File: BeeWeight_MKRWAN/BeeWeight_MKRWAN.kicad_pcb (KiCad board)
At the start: 2 copper layers, 38.6 x 67.9 mm, 34 parts, among them J2 691412120004B, J3 691412120004B, J4 691412120004B, J5 691412120004B, J6 Conn_01x02_Male, J7 Conn_01x14_Female, J8 Conn_01x14_Female, J9 694108301002, Q1 IRLML2244, U1 ADS1241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

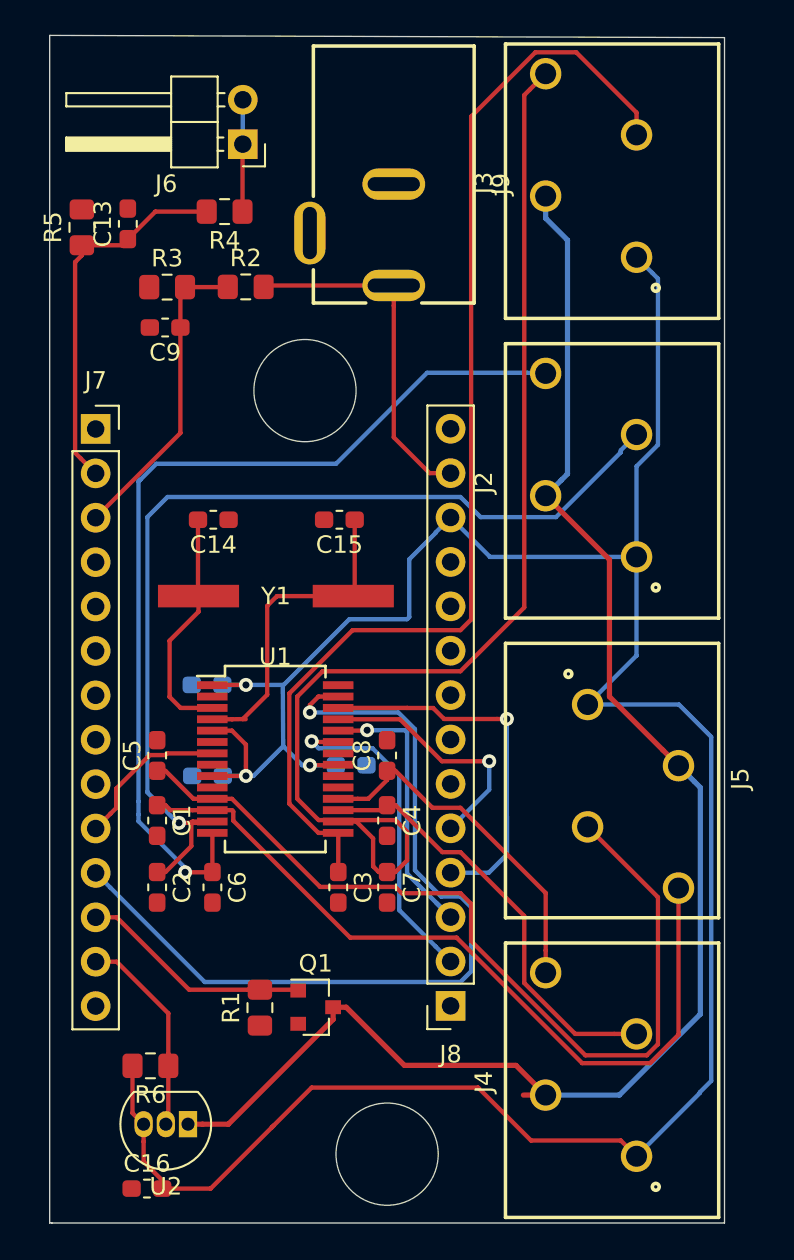
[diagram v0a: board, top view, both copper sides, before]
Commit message: Update Crystal Footprint
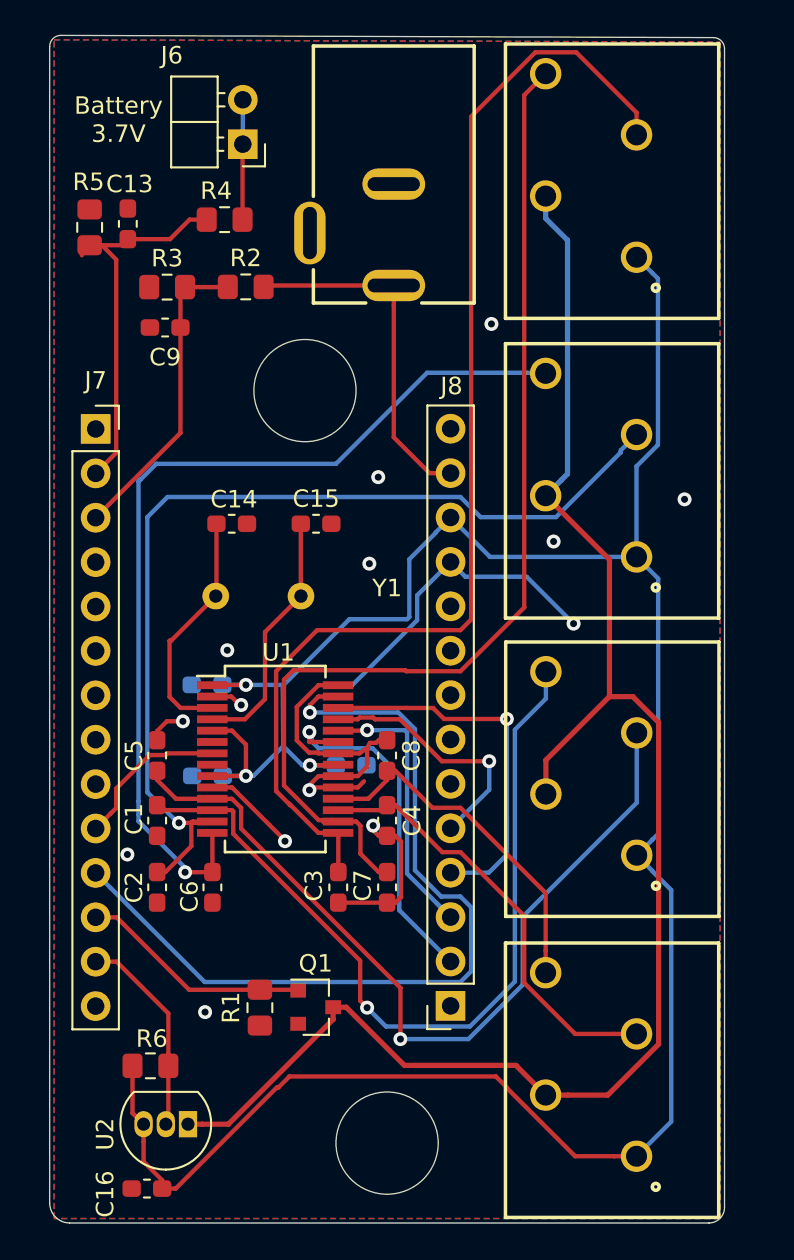
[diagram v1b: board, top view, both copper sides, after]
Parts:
- Y1: footprint USMB_Syl_Mont:Crystal_4Mhz_MCRSD04000F183000RR -> USMB_Syl_Mont:Crystal-4Mhz-TH-Wurth-830027298B
- moved J5 3.04 mm to (182.0, 91.3), turned to 90 degrees
- moved C15 1.35 mm to (166.2, 77.6), turned to 0 degrees
- moved C14 1.08 mm to (161.4, 77.6)
- moved Y1 1.00 mm to (162.9, 81.7)
- moved R4 0.46 mm to (161.0, 60.2)
- moved R5 0.44 mm to (153.3, 60.6)
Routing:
- net GND: track 0.21 -> 56.8 mm, vias 0 -> 14
- net /3V3: track 151.7 -> 145.8 mm
- net /AIN7: track 67.0 -> 61.5 mm
- net /GND_LowPower: track 89.3 -> 93.5 mm
- net Net-(C15-Pad1): track 18.5 -> 14.4 mm
- net /AIN0: track 51.0 -> 48.4 mm, vias 0 -> 1
- net /AIN6: track 66.7 -> 68.7 mm
- net /AIN1: track 45.3 -> 47.3 mm, vias 0 -> 1
- net /D7_CS: track 19.2 -> 20.6 mm
- net /A0_D15_3V7_BAT: track 21.6 -> 22.9 mm
- added copper zone on B.Cu, net GND
- added copper zone on F.Cu, net GND
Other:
- outline, holes or cut-outs redrawn
- board text added: "AIN0"
- board text added: "AIN1"
- board text added: "AIN2"
- board text added: "AIN3"
- board text added: "AIN4"
- board text added: "AIN5"
- board text added: "AIN6"
- board text added: "AIN7"
- board text added: "Alim+"
- board text added: "Alim-"
- board text added: "Battery 3.7V"
- board text added: "Bee Weight MKRWAN Univ Savoie Mont Blanc Version 1"
- board text added: "Diff+"
- board text added: "Diff-"
- board text added: "Solar Panel"

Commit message: Minor changes in schematic and PCB
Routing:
- net /D2_DRDY: track 48.8 -> 46.3 mm
- net /3V3: track 145.8 -> 143.9 mm
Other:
- board text added: "Solar Panel or 4V-17V DC"
- board text removed: "Solar Panel"
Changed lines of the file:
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@@
     (thickness 1.6)
     (drawings 44)
-    (tracks 385)
+    (tracks 384)
     (zones 0)
     (modules 34)
@@
   (layers
     (0 F.Cu signal)
-    (31 B.Cu signal)
+    (31 B.Cu signal hide)
     (32 B.Adhes user)
     (33 F.Adhes user)
@@
     (effects (font (size 1 1) (thickness 0.15)))
   )
-  (gr_text "Solar Panel" (at 170.307 51.943) (layer B.SilkS)
+  (gr_text "Solar Panel\nor\n4V-17V DC" (at 170.688 53.721) (layer B.SilkS)
     (effects (font (size 1 1) (thickness 0.15)) (justify mirror))
   )
@@
   (segment (start 160.3062 92.684) (end 161.4312 92.684) (width 0.25) (layer F.Cu) (net 1))
   (segment (start 161.4312 92.684) (end 164.465 95.7178) (width 0.25) (layer F.Cu) (net 1))
-  (segment (start 172.027009 83.117401) (end 168.27641 86.868) (width 0.25) (layer B.Cu) (net 1))
   (segment (start 173.9392 79.7814) (end 172.02701 81.69359) (width 0.25) (layer B.Cu) (net 1))
-  (segment (start 172.02701 81.69359) (end 172.027009 83.117401) (width 0.25) (layer B.Cu) (net 1))
   (segment (start 168.27641 86.868) (end 167.64 86.868) (width 0.25) (layer B.Cu) (net 1))
   (segment (start 170.307 90.3582) (end 170.307 89.9808) (width 0.25) (layer F.Cu) (net 1))
@@
   (segment (start 168.6312 92.684) (end 168.9862 92.329) (width 0.25) (layer F.Cu) (net 1))
   (segment (start 167.5062 92.684) (end 168.6312 92.684) (width 0.25) (layer F.Cu) (net 1))
+  (segment (start 172.02701 81.69359) (end 172.02701 81.71899) (width 0.25) (layer B.Cu) (net 1))
+  (segment (start 172.02701 81.71899) (end 168.91 84.836) (width 0.25) (layer B.Cu) (net 1))
+  (segment (start 168.91 84.836) (end 168.91 86.36) (width 0.25) (layer B.Cu) (net 1))
+  (segment (start 168.91 86.36) (end 168.27641 86.868) (width 0.25) (layer B.Cu) (net 1))
   (segment (start 175.049201 106.356401) (end 170.237401 106.356401) (width 0.25) (layer B.Cu) (net 2))
   (segment (start 177.61501 103.790592) (end 175.049201 106.356401) (width 0.25) (layer B.Cu) (net 2))
@@
   (segment (start 162.2298 90.2326) (end 162.2298 91.458515) (width 0.25) (layer F.Cu) (net 11))
   (segment (start 160.3062 89.434) (end 161.4312 89.434) (width 0.25) (layer F.Cu) (net 11))
-  (segment (start 173.089201 78.091399) (end 173.089201 78.116799) (width 0.25) (layer B.Cu) (net 11))
-  (segment (start 173.9392 77.2414) (end 173.089201 78.091399) (width 0.25) (layer B.Cu) (net 11))
-  (segment (start 173.089201 78.116799) (end 171.577 79.629) (width 0.25) (layer B.Cu) (net 11))
-  (segment (start 171.577 79.629) (end 171.577 82.931) (width 0.25) (layer B.Cu) (net 11))
-  (segment (start 171.577 82.931) (end 171.45 83.058) (width 0.25) (layer B.Cu) (net 11))
-  (segment (start 171.45 83.058) (end 168.148 83.058) (width 0.25) (layer B.Cu) (net 11))
-  (segment (start 168.148 83.058) (end 164.338 86.868) (width 0.25) (layer B.Cu) (net 11))
   (segment (start 164.3634 86.8172) (end 164.338 86.868) (width 0.25) (layer B.Cu) (net 11))
   (segment (start 164.338 86.868) (end 164.3634 90.3224) (width 0.25) (layer B.Cu) (net 11))
@@
   (segment (start 164.719 109.22) (end 176.53 109.22) (width 0.25) (layer F.Cu) (net 11))
   (segment (start 177.165 109.855) (end 177.136098 109.855) (width 0.25) (layer F.Cu) (net 11))
+  (segment (start 173.089201 78.116799) (end 168.148 83.058) (width 0.25) (layer B.Cu) (net 11))
+  (segment (start 173.9392 77.2414) (end 173.089201 78.091399) (width 0.25) (layer B.Cu) (net 11))
+  (segment (start 168.148 83.058) (end 164.338 86.868) (width 0.25) (layer B.Cu) (net 11))
+  (segment (start 173.089201 78.091399) (end 173.089201 78.116799) (width 0.25) (layer B.Cu) (net 11))
   (segment (start 155.1234 61.6643) (end 155.4734 61.3143) (width 0.25) (layer F.Cu) (net 12))
   (segment (start 152.8445 61.6643) (end 155.1234 61.6643) (width 0.25) (layer F.Cu) (net 12))
@@
   (segment (start 154.806901 92.753189) (end 154.806901 93.859099) (width 0.25) (layer F.Cu) (net 24))
   (segment (start 160.3062 90.734) (end 157.71711 90.734) (width 0.25) (layer F.Cu) (net 24))
-  (segment (start 166.3812 87.484) (end 166.3622 87.503) (width 0.25) (layer F.Cu) (net 25))
-  (segment (start 167.5062 87.484) (end 166.3812 87.484) (width 0.25) (layer F.Cu) (net 25))
-  (via (at 165.887399 88.392) (size 0.8) (drill 0.4) (layers F.Cu B.Cu) (net 25))
-  (segment (start 166.3622 87.503) (end 165.887399 87.977801) (width 0.25) (layer F.Cu) (net 25))
-  (segment (start 165.887399 87.977801) (end 165.887399 88.392) (width 0.25) (layer F.Cu) (net 25))
   (segment (start 175.114201 103.205401) (end 174.503201 103.816401) (width 0.25) (layer B.Cu) (net 25))
   (segment (start 159.874201 103.816401) (end 154.481899 98.424099) (width 0.25) (layer B.Cu) (net 25))
@@
   (segment (start 174.503201 103.816401) (end 159.874201 103.816401) (width 0.25) (layer B.Cu) (net 25))
   (segment (start 171.90001 89.3486) (end 171.90001 97.4258) (width 0.25) (layer B.Cu) (net 25))
-  (segment (start 170.94341 88.392) (end 171.90001 89.3486) (width 0.25) (layer B.Cu) (net 25))
   (segment (start 154.481899 98.424099) (end 153.6319 97.5741) (width 0.25) (layer B.Cu) (net 25))
-  (segment (start 165.887399 88.392) (end 170.94341 88.392) (width 0.25) (layer B.Cu) (net 25))
+  (segment (start 167.5062 87.484) (end 171.431 87.484) (width 0.25) (layer F.Cu) (net 25))
+  (via (at 171.47844 87.409726) (size 0.8) (drill 0.4) (layers F.Cu B.Cu) (net 25))
+  (segment (start 171.431 87.484) (end 171.431 87.457166) (width 0.25) (layer F.Cu) (net 25))
+  (segment (start 171.431 87.457166) (end 171.47844 87.409726) (width 0.25) (layer F.Cu) (net 25))
+  (segment (start 171.90001 88.396981) (end 171.90001 89.3486) (width 0.25) (layer B.Cu) (net 25))
+  (segment (start 171.47844 87.975411) (end 171.90001 88.396981) (width 0.25) (layer B.Cu) (net 25))
+  (segment (start 171.47844 87.409726) (end 171.47844 87.975411) (width 0.25) (layer B.Cu) (net 25))
   (segment (start 162.3299 104.258) (end 163.0299 104.258) (width 0.25) (layer F.Cu) (net 26))
   (segment (start 158.977881 104.258) (end 162.3299 104.258) (width 0.25) (layer F.Cu) (net 26))

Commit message: Nouveau routage par G.Manusset
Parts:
- added JP1: SolderJumper_2_Open, Jumper:SolderJumper-2_P1.3mm_Open_RoundedPad1.0x1.5mm, F.Cu at (164.5, 114.8)
- Q1: value IRLML2244 -> IRLML6244
- moved J3 51.3 mm to (182.2, 108.3)
- moved J4 17.0 mm to (182.0, 91.5)
- moved J5 16.8 mm to (182.0, 74.5)
- moved J2 16.7 mm to (182.0, 57.5)
- moved C2 16.4 mm to (159.1, 82.2), turned to 180 degrees
- moved C1 14.3 mm to (161.7, 81.0), turned to 90 degrees
- moved C6 13.5 mm to (158.2, 85.1)
- moved C11 13.1 mm to (165.5, 80.1), turned to 270 degrees
- moved C3 12.2 mm to (158.2, 90.6), turned to 90 degrees
- moved C7 12.2 mm to (159.1, 93.7), turned to 180 degrees
- moved C10 12.1 mm to (170.0, 80.0), turned to 270 degrees
- moved C5 11.7 mm to (163.4, 81.0)
- moved C4 8.64 mm to (161.7, 95.3)
- moved C14 8.43 mm to (169.4, 80.2)
- moved U1 8.19 mm to (171.4, 87.9), turned to 270 degrees
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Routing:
- net /AIN7: track 61.5 -> 32.1 mm
- net GND: track 56.9 -> 27.6 mm, vias 14 -> 3
- net /D2_DRDY: track 46.3 -> 18.9 mm
- net /AIN6: track 68.7 -> 42.5 mm
- net /AIN2: track 24.9 -> 45.7 mm
- net /AIN3: track 20.3 -> 38.9 mm
- net /AIN1: track 47.3 -> 31.9 mm, vias 1 -> 0
- net /GND_LowPower: track 93.5 -> 79.6 mm, vias 0 -> 1
- net /AIN0: track 48.4 -> 35.4 mm, vias 1 -> 0
- net /AIN4: track 56.3 -> 43.7 mm, vias 1 -> 0
- net /D9_SCLK: track 21.3 -> 11.2 mm, vias 1 -> 0
- net /D1_PDWN: track 9.10 -> 17.2 mm, vias 0 -> 1
- net /A0_D15_3V7_BAT: track 22.9 -> 15.4 mm
- net /Vin: track 20.3 -> 27.1 mm
- net /D7_CS: track 20.6 -> 14.4 mm, vias 1 -> 0
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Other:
- outline, holes or cut-outs redrawn

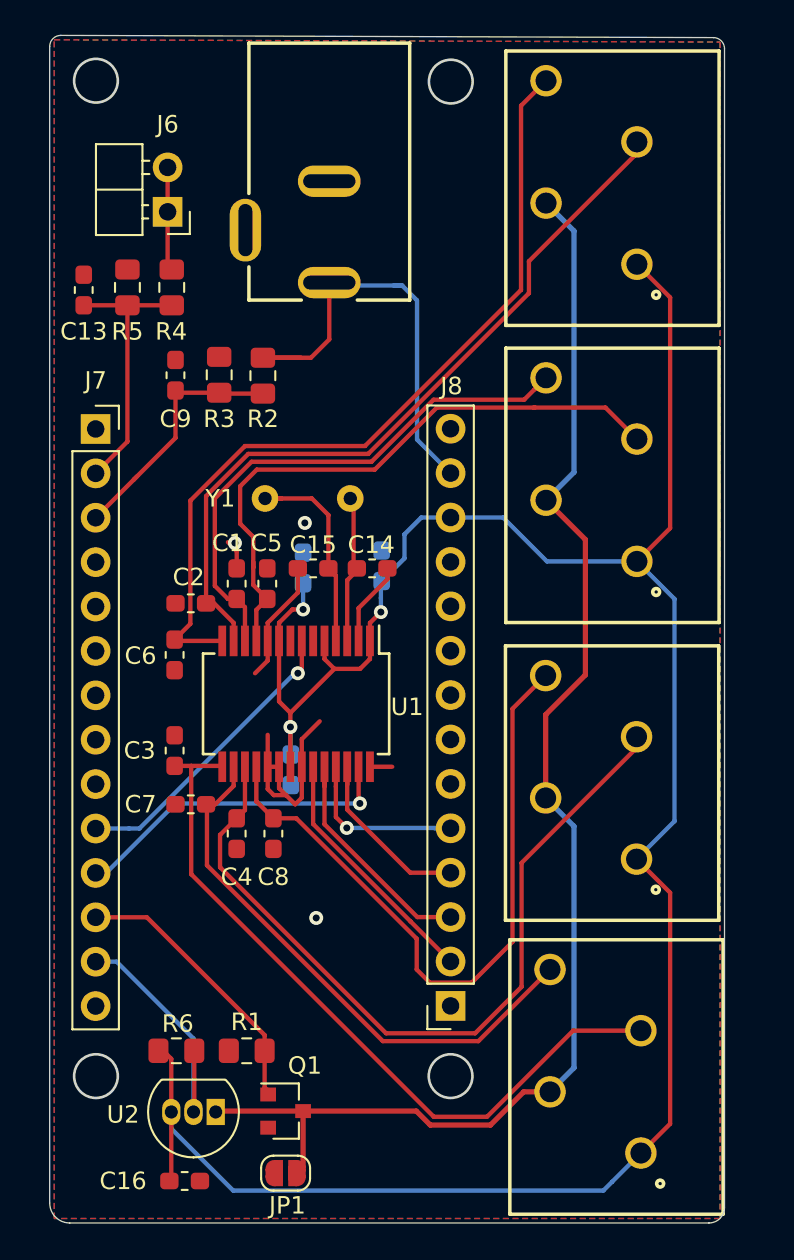
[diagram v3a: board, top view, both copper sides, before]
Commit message: Update DS18B20 Footprint
Otherwise eurocircuit fees are based on class 8 PCB
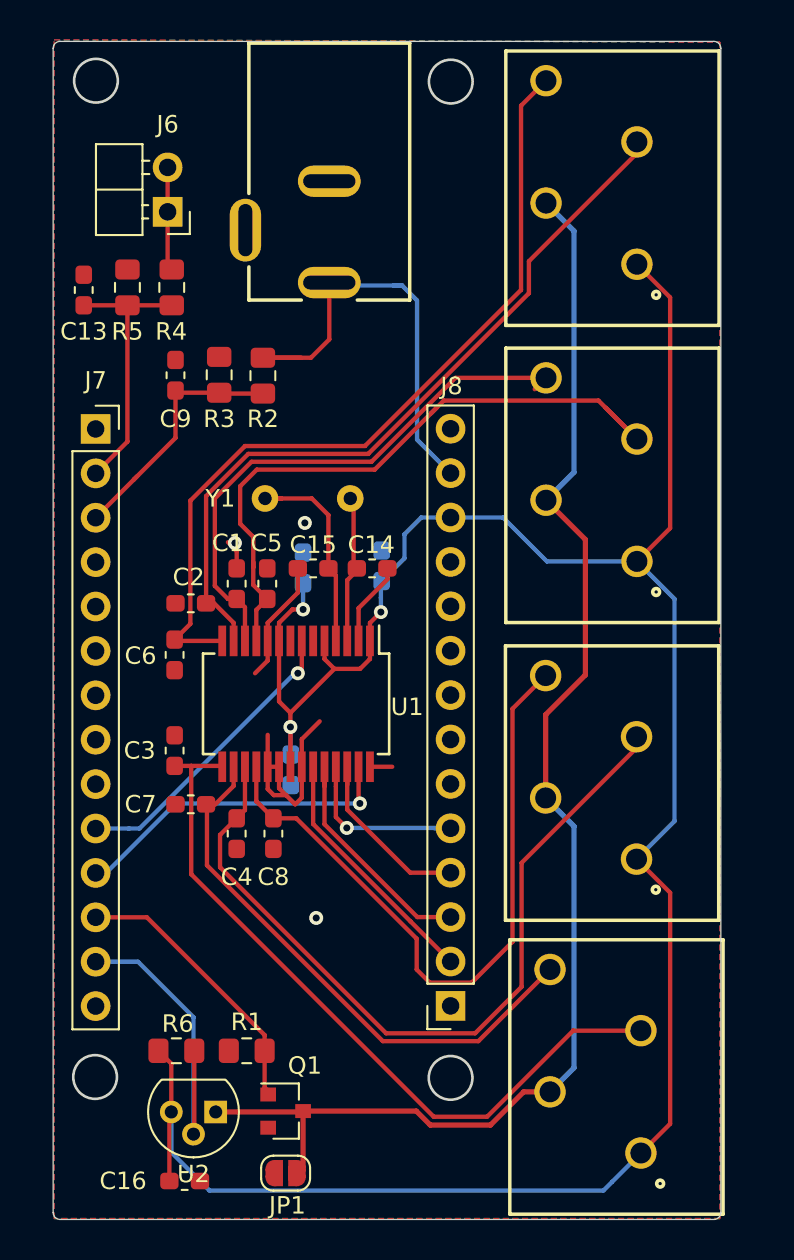
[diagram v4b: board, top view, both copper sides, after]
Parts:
- U2: footprint Package_TO_SOT_THT:TO-92_Inline -> Package_TO_SOT_THT:TO-92
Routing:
- net /AIN0: track 35.4 -> 38.7 mm
- net /D4_DS1820_DQ: track 15.1 -> 18.4 mm
- net /3V3: track 137.8 -> 139.0 mm
- net /GND_LowPower: vias 1 -> 0
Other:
- board size 38.6 x 67.9 mm -> 38.2 x 67.4 mm
- board text added: "Batt 3.7V"
- board text removed: "Battery 3.7V"
